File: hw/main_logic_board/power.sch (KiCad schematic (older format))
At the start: 5 parts, among them J1 BATT_IN, J2 PWR_SEL, U4 LM1085-5.0

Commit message: Finish initial power schematics, swap some footprints for visualization in pcb view
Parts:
- added C10, C11, C12, C7, C9: 10u, symbol Device:C_Small
- added C13, C14: 100n, symbol Device:C_Small
- added C15, C16, C17, C18, C19: 22u, symbol Device:C_Small
- added C8: 100u, symbol Device:C_Small
- added F1: Fuse, symbol Device:Fuse
- added J3: 3V3_PWR_SEL, Jumper:SolderJumper-3_P1.3mm_Open_Pad1.0x1.5mm, symbol Connector_Generic:Conn_01x03
- added L1: 3.3u 20mOhm, symbol Device:L_Small
- added L2: 2.2u 15mOhm, symbol Device:L_Small
- added R1: 56.2k, symbol Device:R_Small_US
- added R2, R4: 10k, symbol Device:R_Small_US
- added R3: 33.2k, symbol Device:R_Small_US
- added U5: LM1085-3.3, Package_TO_SOT_SMD:TO-263-3_TabPin2, symbol Regulator_Linear:LM1085-3.3
- added U6, U7: TPS563200, Package_TO_SOT_SMD:SOT-23-6, symbol Regulator_Switching:TPS563200
- C2: value C_Small -> 10u
- C3: value C_Small -> 100u
- J2: value PWR_SEL -> 5V_PWR_SEL; footprint Connector_PinHeader_2.54mm:PinHeader_1x03_P2.54mm_Vertical -> Jumper:SolderJumper-3_P1.3mm_Open_Pad1.0x1.5mm
- U4: footprint (none) -> Package_TO_SOT_SMD:TO-263-3_TabPin2
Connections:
- net labels added: +3V3
- wire segments 20 -> 123
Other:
- note added: "Layout Guidelines for LM1085"
- note added: "Layout Guidelines for TPS563200"
- note added: "Tantalum"
- moved on the sheet: J1

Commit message: Finish prelim schematic + PCB component placement
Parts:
- removed U4: LM1085-5.0, Package_TO_SOT_SMD:TO-263-3_TabPin2, symbol Regulator_Linear:LM1085-5.0
- removed U5: LM1085-3.3, Package_TO_SOT_SMD:TO-263-3_TabPin2, symbol Regulator_Linear:LM1085-3.3
- added U4: NCP1117-5.0_SOT223, Package_TO_SOT_SMD:SOT-223-3_TabPin2, symbol Regulator_Linear:NCP1117-5.0_SOT223
- added U5: NCP1117-3.3_SOT223, Package_TO_SOT_SMD:SOT-223-3_TabPin2, symbol Regulator_Linear:NCP1117-3.3_SOT223
- C10, C11, C12, C13, C14, C15, C16, C17, C18, C19, C2, C7, C9: footprint (none) -> Capacitor_SMD:C_0805_2012Metric
- C3, C8: value 100u -> 10u; footprint (none) -> Capacitor_SMD:C_0805_2012Metric
- J1: footprint Connector_Wire:SolderWirePad_1x02_P7.62mm_Drill2mm -> Connector_Wire:SolderWirePad_1x02_P5.08mm_Drill1.5mm
- L1: footprint (none) -> Inductor_SMD:L_Abracon_ASPI-0630LR
- L2: footprint (none) -> Inductor_SMD:L_Vishay_IHLP-2020
- R1, R2, R3, R4: footprint (none) -> Resistor_SMD:R_0805_2012Metric
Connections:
- net labels added: +BATT
- wire segments 123 -> 124
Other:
- note removed: "Layout Guidelines for LM1085"
- note removed: "Tantalum"

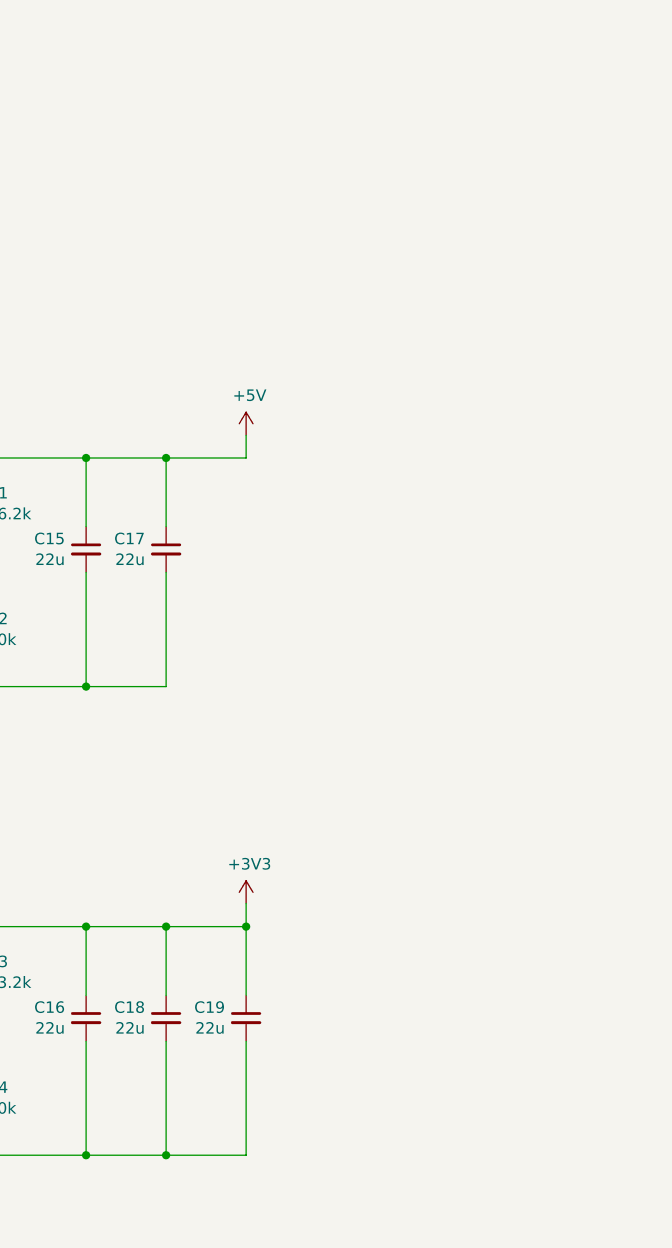
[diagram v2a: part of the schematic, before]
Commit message: Add debug headers, LED wiring, remove MPU
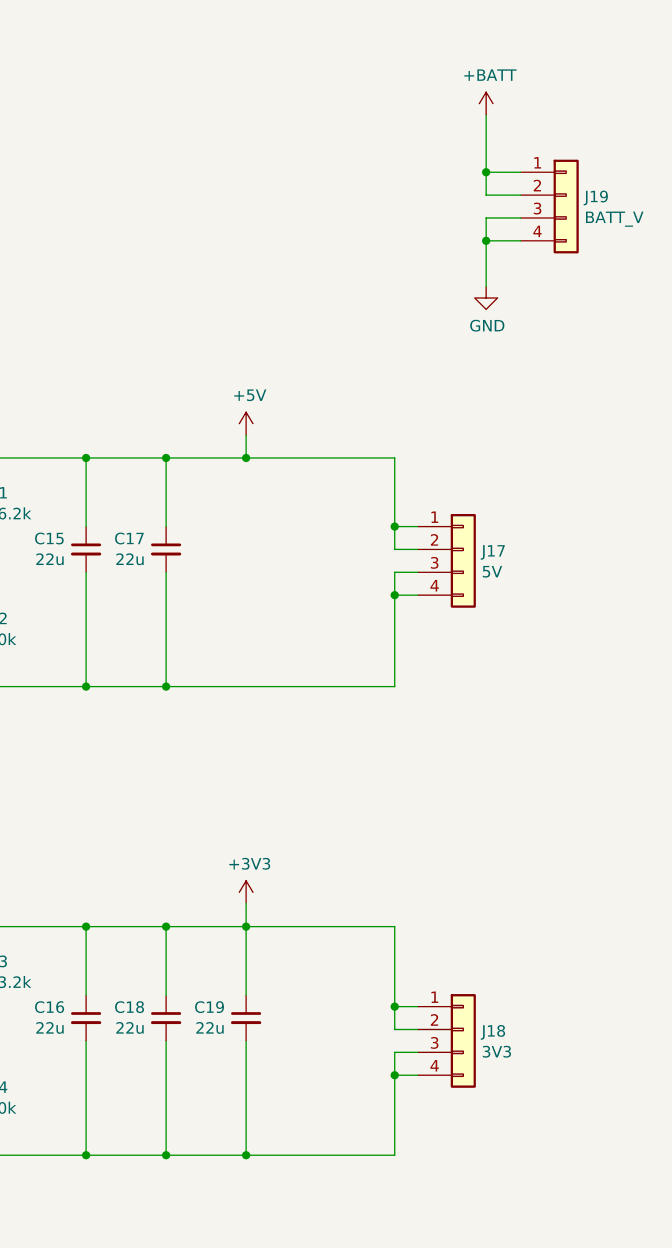
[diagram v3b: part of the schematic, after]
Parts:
- added J17: 5V, Connector_PinHeader_1.27mm:PinHeader_1x04_P1.27mm_Vertical, symbol Connector_Generic:Conn_01x04
- added J18: 3V3, Connector_PinHeader_1.27mm:PinHeader_1x04_P1.27mm_Vertical, symbol Connector_Generic:Conn_01x04
- added J19: BATT_V, Connector_PinHeader_1.27mm:PinHeader_1x04_P1.27mm_Vertical, symbol Connector_Generic:Conn_01x04
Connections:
- net +3V3: now also J18.1 (Pin_1), J18.2 (Pin_2)
- net +5V: now also J17.1 (Pin_1), J17.2 (Pin_2)
- net +BATT: now also J19.1 (Pin_1), J19.2 (Pin_2)
- net GND: now also J17.3 (Pin_3), J17.4 (Pin_4), J18.3 (Pin_3), J18.4 (Pin_4), J19.3 (Pin_3), J19.4 (Pin_4)

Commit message: Add 3D model files, lay out switching circuit, other tweaks
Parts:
- F1: footprint (none) -> Fuse:Fuse_1206_3216Metric
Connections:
- net BATT_VIN_5V: now reaches C11.1, C9.1, J2.1 (Pin_1), U6.3 (VIN), U6.5 (EN)
- net BATT_VIN_3V3: now reaches C10.1, C12.1, J3.1 (Pin_1), U7.3 (VIN), U7.5 (EN)
- net SW_NODE_5V: now reaches C13.1, L1.1, U6.2 (SW)
- net SW_NODE_3V3: now reaches C14.1, L2.1, U7.2 (SW)
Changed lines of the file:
@@
 F 0 "F1" V 1003 1150 50  0000 C CNN
 F 1 "Fuse" V 1094 1150 50  0000 C CNN
-F 2 "" V 1130 1150 50  0001 C CNN
+F 2 "Fuse:Fuse_1206_3216Metric" V 1130 1150 50  0001 C CNN
 F 3 "~" H 1200 1150 50  0001 C CNN
 	1    1200 1150
@@
 	1    0    0    -1
 $EndComp
+Text Label 2550 2500 0    50   ~ 0
+BATT_VIN_5V
+Text Label 2550 4550 0    50   ~ 0
+BATT_VIN_3V3
+Text Label 6950 2500 0    50   ~ 0
+SW_NODE_5V
+Text Label 6900 4550 0    50   ~ 0
+SW_NODE_3V3
 $EndSCHEMATC

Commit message: Add power + GPIO LEDs
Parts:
- added D10: 3V3_RED, Diode_SMD:D_0805_2012Metric, symbol Device:LED
- added D9: 5V_RED, Diode_SMD:D_0805_2012Metric, symbol Device:LED
- added R18, R19: 1K, Resistor_SMD:R_0805_2012Metric, symbol Device:R_Small_US
- R1: value 56.2k -> 56.2K 1%
- R2, R4: value 10k -> 10K 1%
- R3: value 33.2k -> 33.2K 1%
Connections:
- net +3V3: now also R19.1
- net +5V: now also R18.1
- net GND: now also D10.1 (K), D9.1 (K)
- new net: D9.2 (A), R18.2
- new net: D10.2 (A), R19.2
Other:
- moved on the sheet: J17, J18
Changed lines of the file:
@@
 F 1 "Fuse" V 1094 1150 50  0000 C CNN
 F 2 "Fuse:Fuse_1206_3216Metric" V 1130 1150 50  0001 C CNN
-F 3 "~" H 1200 1150 50  0001 C CNN
+F 3 "https://www.digikey.ca/product-detail/en/bel-fuse-inc/0685P9400-01/507-2460-1-ND/10057403" H 1200 1150 50  0001 C CNN
 	1    1200 1150
 	0    1    1    0
@@
 AR Path="/5EB4BC23/5EA8994C" Ref="L?"  Part="1"
 F 0 "L1" V 7735 2500 50  0000 C CNN
-F 1 "3.3u 20mOhm" V 7644 2500 50  0000 C CNN
+F 1 "3.3u 20mOhm" V 7650 2300 50  0000 C CNN
 F 2 "Inductor_SMD:L_Abracon_ASPI-0630LR" H 7550 2500 50  0001 C CNN
 F 3 "https://www.digikey.ca/product-detail/en/abracon-llc/ASPI-0630LR-3R3M-T15/ASPI-0630LR-3R3M-T15CT-ND/3060139" H 7550 2500 50  0001 C CNN
@@
 AR Path="/5EB4BC23/5EA8D2F6" Ref="R?"  Part="1"
 F 0 "R1" H 7918 2746 50  0000 L CNN
-F 1 "56.2k" H 7918 2655 50  0000 L CNN
+F 1 "56.2K 1%" H 7918 2655 50  0000 L CNN
 F 2 "Resistor_SMD:R_0805_2012Metric" H 7850 2700 50  0001 C CNN
 F 3 "~" H 7850 2700 50  0001 C CNN
@@
 AR Path="/5EB4BC23/5EA8E302" Ref="R?"  Part="1"
 F 0 "R2" H 7918 3296 50  0000 L CNN
-F 1 "10k" H 7918 3205 50  0000 L CNN
+F 1 "10K 1%" H 7918 3205 50  0000 L CNN
 F 2 "Resistor_SMD:R_0805_2012Metric" H 7850 3250 50  0001 C CNN
 F 3 "~" H 7850 3250 50  0001 C CNN
@@
 AR Path="/5EB4BC23/5EAAF5AA" Ref="L?"  Part="1"
 F 0 "L2" V 7735 4550 50  0000 C CNN
-F 1 "2.2u 15mOhm" V 7644 4550 50  0000 C CNN
+F 1 "2.2u 15mOhm" V 7650 4350 50  0000 C CNN
 F 2 "Inductor_SMD:L_Vishay_IHLP-2020" H 7550 4550 50  0001 C CNN
 F 3 "https://www.digikey.ca/product-detail/en/vishay-dale/IHLP2020CZER2R2M11/541-1236-1-ND/2025126" H 7550 4550 50  0001 C CNN
@@
 AR Path="/5EB4BC23/5EAAF5BA" Ref="R?"  Part="1"
 F 0 "R3" H 7918 4796 50  0000 L CNN
-F 1 "33.2k" H 7918 4705 50  0000 L CNN
+F 1 "33.2K 1%" H 7918 4705 50  0000 L CNN
 F 2 "Resistor_SMD:R_0805_2012Metric" H 7850 4750 50  0001 C CNN
 F 3 "~" H 7850 4750 50  0001 C CNN
@@
 AR Path="/5EB4BC23/5EAAF5C0" Ref="R?"  Part="1"
 F 0 "R4" H 7918 5346 50  0000 L CNN
-F 1 "10k" H 7918 5255 50  0000 L CNN
+F 1 "10K 1%" H 7918 5255 50  0000 L CNN
 F 2 "Resistor_SMD:R_0805_2012Metric" H 7850 5300 50  0001 C CNN
 F 3 "~" H 7850 5300 50  0001 C CNN
@@
 L Connector_Generic:Conn_01x04 J17
 U 1 1 5EBE6D7A
-P 10000 2900
-F 0 "J17" H 10080 2892 50  0000 L CNN
-F 1 "5V" H 10080 2801 50  0000 L CNN
-F 2 "Connector_PinHeader_1.27mm:PinHeader_1x04_P1.27mm_Vertical" H 10000 2900 50  0001 C CNN
-F 3 "~" H 10000 2900 50  0001 C CNN
-	1    10000 2900
+P 10150 2900
+F 0 "J17" H 10230 2892 50  0000 L CNN
+F 1 "5V" H 10230 2801 50  0000 L CNN
+F 2 "Connector_PinHeader_1.27mm:PinHeader_1x04_P1.27mm_Vertical" H 10150 2900 50  0001 C CNN
+F 3 "~" H 10150 2900 50  0001 C CNN
+	1    10150 2900
 	1    0    0    -1
 $EndComp
@@
 L Connector_Generic:Conn_01x04 J18
 U 1 1 5EBEACCC
-P 10000 5000
-F 0 "J18" H 10080 4992 50  0000 L CNN
-F 1 "3V3" H 10080 4901 50  0000 L CNN
-F 2 "Connector_PinHeader_1.27mm:PinHeader_1x04_P1.27mm_Vertical" H 10000 5000 50  0001 C CNN
-F 3 "~" H 10000 5000 50  0001 C CNN
-	1    10000 5000
-	1    0    0    -1
-$EndComp
-Wire Wire Line
-	8700 3500 9700 3500
-Wire Wire Line
-	9700 3500 9700 3100
-Wire Wire Line
-	9700 3000 9800 3000
+P 10150 5000
+F 0 "J18" H 10230 4992 50  0000 L CNN
+F 1 "3V3" H 10230 4901 50  0000 L CNN
+F 2 "Connector_PinHeader_1.27mm:PinHeader_1x04_P1.27mm_Vertical" H 10150 5000 50  0001 C CNN
+F 3 "~" H 10150 5000 50  0001 C CNN
+	1    10150 5000
+	1    0    0    -1
+$EndComp
+Wire Wire Line
+	8700 3500 9250 3500
+Wire Wire Line
+	9850 3500 9850 3100
+Wire Wire Line
+	9850 3000 9950 3000
 Connection ~ 8700 3500
 Wire Wire Line
-	9700 3100 9800 3100
-Connection ~ 9700 3100
-Wire Wire Line
-	9700 3100 9700 3000
-Wire Wire Line
-	9800 2900 9700 2900
-Wire Wire Line
-	9700 2900 9700 2800
-Wire Wire Line
-	9700 2500 9050 2500
+	9850 3100 9950 3100
+Connection ~ 9850 3100
+Wire Wire Line
+	9850 3100 9850 3000
+Wire Wire Line
+	9950 2900 9850 2900
+Wire Wire Line
+	9850 2900 9850 2800
 Connection ~ 9050 2500
 Wire Wire Line
-	9800 2800 9700 2800
-Connection ~ 9700 2800
-Wire Wire Line
-	9700 2800 9700 2500
-Wire Wire Line
-	9800 4900 9700 4900
-Wire Wire Line
-	9700 4900 9700 4550
-Wire Wire Line
-	9700 4550 9050 4550
-Wire Wire Line
-	9700 4900 9700 5000
-Wire Wire Line
-	9700 5000 9800 5000
-Connection ~ 9700 4900
-Wire Wire Line
-	9800 5100 9700 5100
-Wire Wire Line
-	9700 5100 9700 5200
-Wire Wire Line
-	9700 5550 9050 5550
+	9950 2800 9850 2800
+Connection ~ 9850 2800
+Wire Wire Line
+	9850 2800 9850 2500
+Wire Wire Line
+	9950 4900 9850 4900
+Wire Wire Line
+	9850 4900 9850 4550
+Wire Wire Line
+	9850 4900 9850 5000
+Wire Wire Line
+	9850 5000 9950 5000
+Connection ~ 9850 4900
+Wire Wire Line
+	9950 5100 9850 5100
+Wire Wire Line
+	9850 5100 9850 5200
 Connection ~ 9050 5550
 Wire Wire Line
-	9800 5200 9700 5200
-Connection ~ 9700 5200
-Wire Wire Line
-	9700 5200 9700 5550
+	9950 5200 9850 5200
+Connection ~ 9850 5200
+Wire Wire Line
+	9850 5200 9850 5550
 $Comp
 L Connector_Generic:Conn_01x04 J19
@@
 Text Label 6900 4550 0    50   ~ 0
 SW_NODE_3V3
+$Comp
+L Device:LED D9
+U 1 1 5EDC0E2B
+P 9250 3200
+F 0 "D9" V 9289 3083 50  0000 R CNN
+F 1 "5V_RED" V 9198 3083 50  0000 R CNN
+F 2 "Diode_SMD:D_0805_2012Metric" H 9250 3200 50  0001 C CNN
+F 3 "~" H 9250 3200 50  0001 C CNN
+	1    9250 3200
+	0    -1   -1   0
+$EndComp
+Wire Wire Line
+	9250 3350 9250 3500
+$Comp
+L Device:LED D10
+U 1 1 5EDC88D3
+P 9350 5250
+F 0 "D10" V 9389 5132 50  0000 R CNN
+F 1 "3V3_RED" V 9298 5132 50  0000 R CNN
+F 2 "Diode_SMD:D_0805_2012Metric" H 9350 5250 50  0001 C CNN
+F 3 "~" H 9350 5250 50  0001 C CNN
+	1    9350 5250
+	0    -1   -1   0
+$EndComp
+Wire Wire Line
+	9350 5550 9350 5400
+Connection ~ 9350 5550
+Wire Wire Line
+	9350 5550 9050 5550
+$Comp
+L Device:R_Small_US R18
+U 1 1 5EDD401C
+P 9250 2750
+AR Path="/5E9DC864/5EDD401C" Ref="R18"  Part="1"
+AR Path="/5EB4BC23/5EDD401C" Ref="R?"  Part="1"
+F 0 "R18" H 9318 2796 50  0000 L CNN
+F 1 "1K" H 9318 2705 50  0000 L CNN
+F 2 "Resistor_SMD:R_0805_2012Metric" H 9250 2750 50  0001 C CNN
+F 3 "~" H 9250 2750 50  0001 C CNN
+	1    9250 2750
+	1    0    0    -1
+$EndComp
+Wire Wire Line
+	9250 3050 9250 2850
+Wire Wire Line
+	9250 2650 9250 2500
+Wire Wire Line
+	9250 2500 9050 2500
+$Comp
+L Device:R_Small_US R19
+U 1 1 5EDECF63
+P 9350 4850
+AR Path="/5E9DC864/5EDECF63" Ref="R19"  Part="1"
+AR Path="/5EB4BC23/5EDECF63" Ref="R?"  Part="1"
+F 0 "R19" H 9418 4896 50  0000 L CNN
+F 1 "1K" H 9418 4805 50  0000 L CNN
+F 2 "Resistor_SMD:R_0805_2012Metric" H 9350 4850 50  0001 C CNN
+F 3 "~" H 9350 4850 50  0001 C CNN
+	1    9350 4850
+	1    0    0    -1
+$EndComp
+Wire Wire Line
+	9350 5100 9350 4950
+Wire Wire Line
+	9350 4750 9350 4550
+Connection ~ 9350 4550
+Wire Wire Line
+	9350 4550 9050 4550
+Wire Wire Line
+	9350 5550 9850 5550
+Wire Wire Line
+	9350 4550 9850 4550
+Wire Wire Line
+	9250 3500 9850 3500
+Connection ~ 9250 3500
+Wire Wire Line
+	9250 2500 9850 2500
+Connection ~ 9250 2500
 $EndSCHEMATC

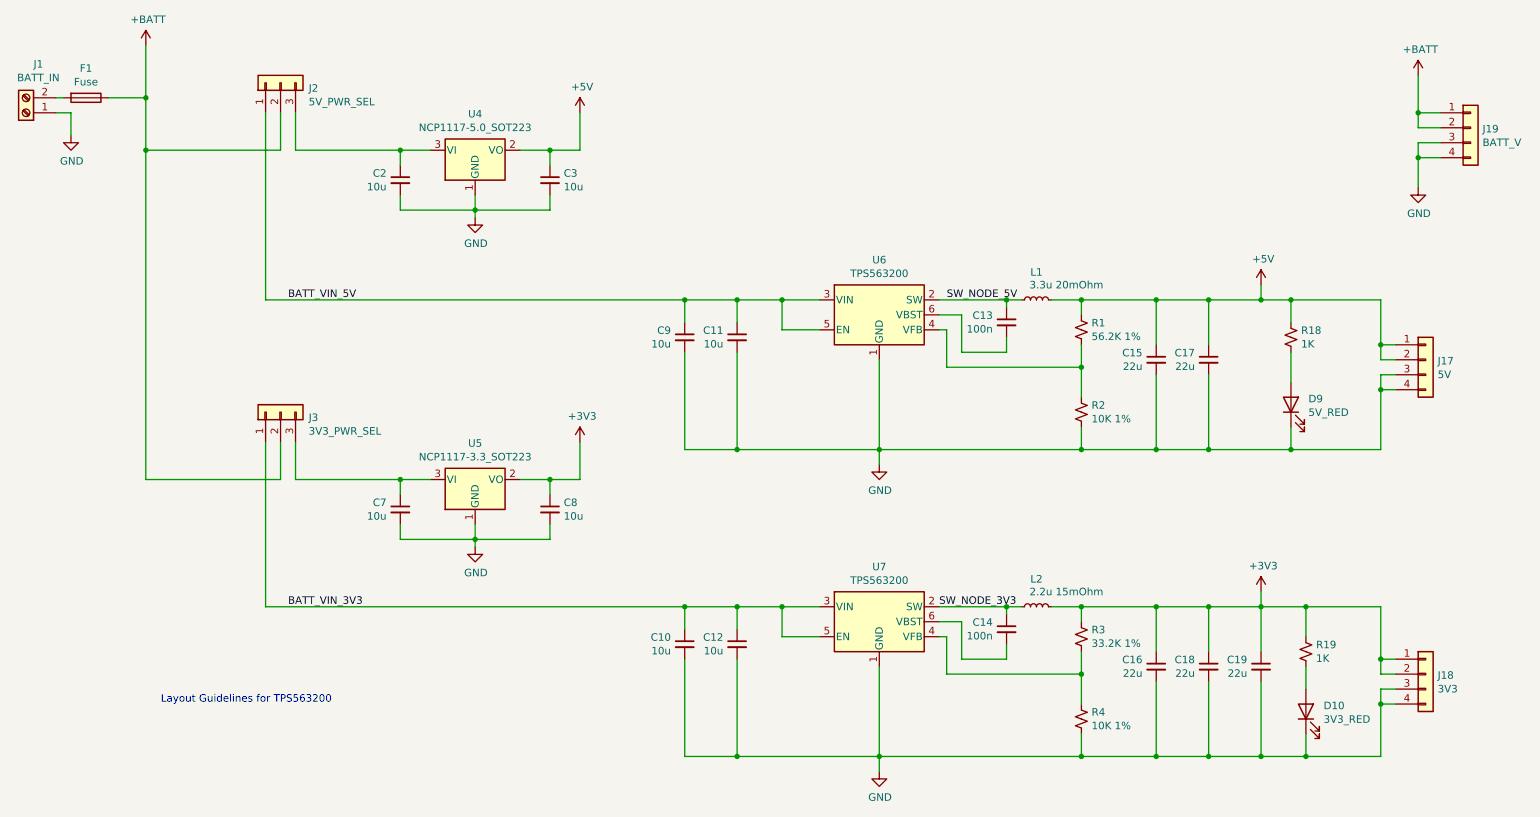
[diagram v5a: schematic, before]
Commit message: Add current sensor, layout progress, and remove temp mech files
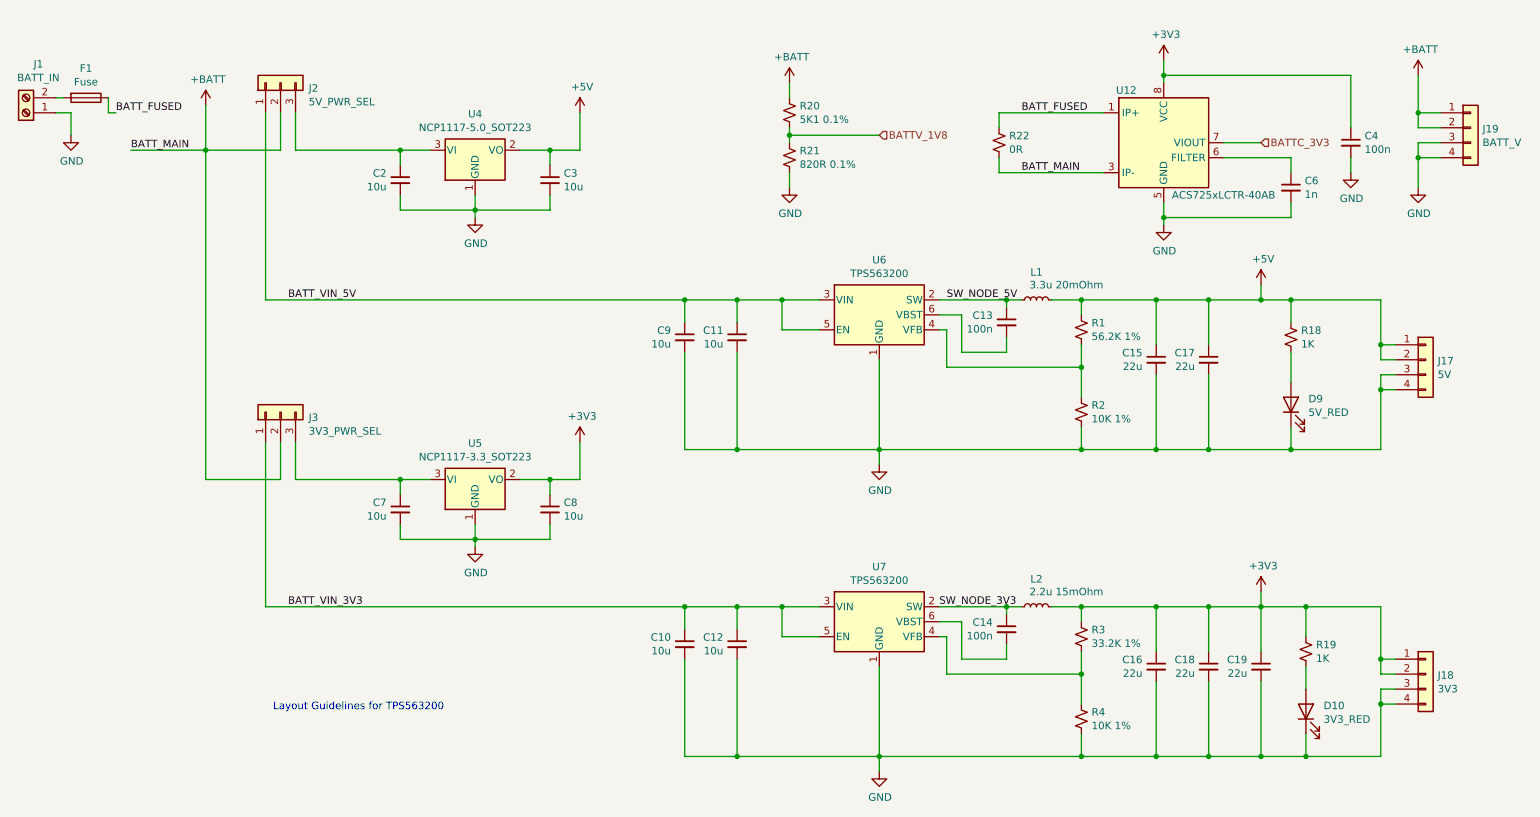
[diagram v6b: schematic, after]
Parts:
- added C4: 100n, Capacitor_SMD:C_0805_2012Metric, symbol Device:C_Small
- added C6: 1n, Capacitor_SMD:C_0805_2012Metric, symbol Device:C_Small
- added R20: 5K1 0.1%, Resistor_SMD:R_0805_2012Metric, symbol Device:R_Small_US
- added R21: 820R 0.1%, Resistor_SMD:R_0805_2012Metric, symbol Device:R_Small_US
- added R22: 0R, Resistor_SMD:R_2816_7142Metric_Pad3.20x4.45mm_HandSolder, symbol Device:R_Small_US
- added U12: ACS725xLCTR-40AB, Package_SO:SOIC-8_3.9x4.9mm_P1.27mm, symbol Sensor_Current:ACS725xLCTR-40AB
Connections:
- net +3V3: now also C4.1, U12.8 (VCC)
- net +BATT: now also R20.1, R22.2, U12.3 (IP-), U12.4 (IP-); no longer F1.1
- net GND: now also C4.2, C6.2, R21.2, U12.5 (GND)
- new net: C6.1, U12.6 (FILTER)
- new net BATTC_3V3: U12.7 (VIOUT)
- new net BATTV_1V8: R20.2, R21.1
- new net BATT_FUSED: F1.1, R22.1, U12.1 (IP+), U12.2 (IP+)

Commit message: Adding BOM information
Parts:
- F1: Digikey (none) -> https://www.digikey.ca/product-detail/en/bel-fuse-inc/0685P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
- L1: Digikey (none) -> https://www.digikey.ca/product-detail/en/abracon-llc/ASPI-0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
- L2: Digikey (none) -> https://www.digikey.ca/product-detail/en/vishay-dale/IHLP20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
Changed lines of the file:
@@
 F 1 "Fuse" V 1094 1150 50  0000 C CNN
 F 2 "Fuse:Fuse_1206_3216Metric" V 1130 1150 50  0001 C CNN
-F 3 "https://www.digikey.ca/product-detail/en/bel-fuse-inc/0685P9400-01/507-2460-1-ND/10057403" H 1200 1150 50  0001 C CNN
+F 3 "~" H 1200 1150 50  0001 C CNN
+F 4 "https://www.digikey.ca/product-detail/en/bel-fuse-inc/0685P9400-01/507-2460-1-ND/10057403" H 1200 1150 50  0001 C CNN "Digikey"
 	1    1200 1150
 	0    1    1    0
@@
 F 1 "3.3u 20mOhm" V 7650 2300 50  0000 C CNN
 F 2 "Inductor_SMD:L_Abracon_ASPI-0630LR" H 7550 2500 50  0001 C CNN
-F 3 "https://www.digikey.ca/product-detail/en/abracon-llc/ASPI-0630LR-3R3M-T15/ASPI-0630LR-3R3M-T15CT-ND/3060139" H 7550 2500 50  0001 C CNN
+F 3 "~" H 7550 2500 50  0001 C CNN
+F 4 "https://www.digikey.ca/product-detail/en/abracon-llc/ASPI-0630LR-3R3M-T15/ASPI-0630LR-3R3M-T15CT-ND/3060139" H 7550 2500 50  0001 C CNN "Digikey"
 	1    7550 2500
 	0    -1   -1   0
@@
 F 1 "2.2u 15mOhm" V 7650 4350 50  0000 C CNN
 F 2 "Inductor_SMD:L_Vishay_IHLP-2020" H 7550 4550 50  0001 C CNN
-F 3 "https://www.digikey.ca/product-detail/en/vishay-dale/IHLP2020CZER2R2M11/541-1236-1-ND/2025126" H 7550 4550 50  0001 C CNN
+F 3 "~" H 7550 4550 50  0001 C CNN
+F 4 "https://www.digikey.ca/product-detail/en/vishay-dale/IHLP2020CZER2R2M11/541-1236-1-ND/2025126" H 7550 4550 50  0001 C CNN "Digikey"
 	1    7550 4550
 	0    -1   -1   0
